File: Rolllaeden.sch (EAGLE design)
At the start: 62 parts, among them IC1 PCF8574P, IC2 PCF8574P, IC3 74HCT04N, IC4 74HCT08N, IC5 74HCT08N, J1 J7MM, J2 J7MM, T1 BC337-25, T2 BC337-25, T3 BC337-25, T4 BC337-25, T5 BC337-25, T6 BC337-25

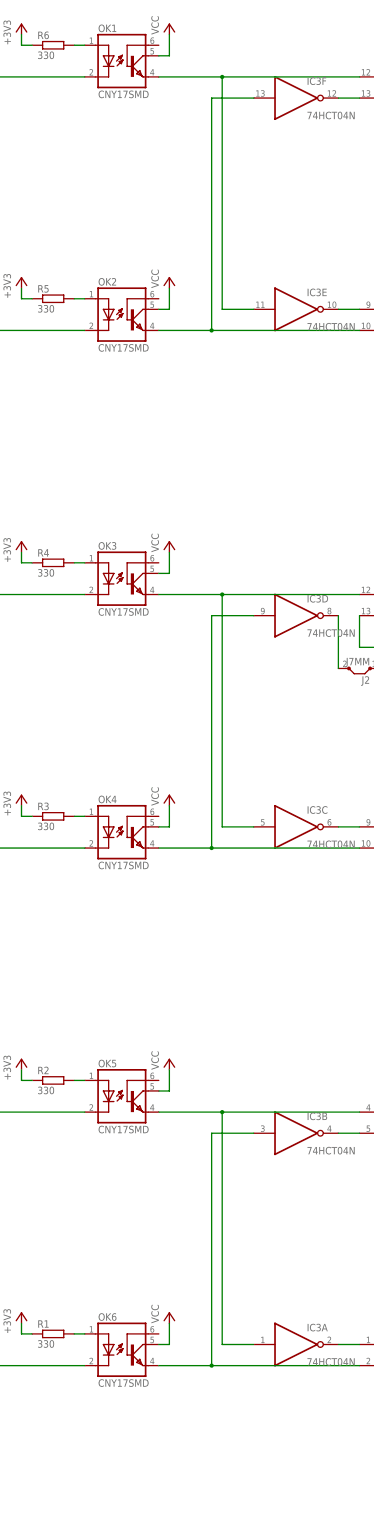
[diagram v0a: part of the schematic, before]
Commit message: Pulldown-Widerstände zwichen Optokopplern und Logik-ICs hinzugefügt
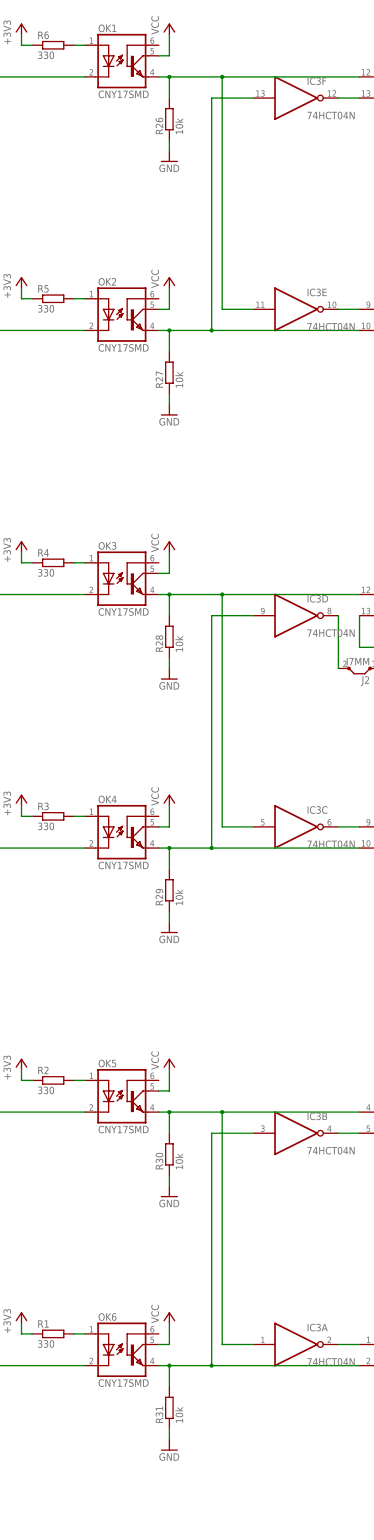
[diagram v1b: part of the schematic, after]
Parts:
- added R26, R27, R28, R29, R30, R31: 10k, resistor:R-EU_0204/2V
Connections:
- net GND: now also R26.1, R27.1, R28.1, R29.1, R30.1, R31.1
- net N$11: now also R30.2
- net N$22: now also R29.2
- net N$23: now also R28.2
- net N$34: now also R27.2
- net N$35: now also R26.2
- net N$4: now also R31.2
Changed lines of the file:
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@@
 <part name="+3V11" library="supply1" deviceset="+3V3" device=""/>
 <part name="F1" library="fuse" deviceset="LITTLEFUSE" device="" value="250mA"/>
+<part name="R26" library="resistor" deviceset="R-EU_" device="0204/2V" value="10k"/>
+<part name="GND5" library="supply1" deviceset="GND" device=""/>
+<part name="R27" library="resistor" deviceset="R-EU_" device="0204/2V" value="10k"/>
+<part name="GND7" library="supply1" deviceset="GND" device=""/>
+<part name="R28" library="resistor" deviceset="R-EU_" device="0204/2V" value="10k"/>
+<part name="GND10" library="supply1" deviceset="GND" device=""/>
+<part name="R29" library="resistor" deviceset="R-EU_" device="0204/2V" value="10k"/>
+<part name="GND11" library="supply1" deviceset="GND" device=""/>
+<part name="R30" library="resistor" deviceset="R-EU_" device="0204/2V" value="10k"/>
+<part name="GND14" library="supply1" deviceset="GND" device=""/>
+<part name="R31" library="resistor" deviceset="R-EU_" device="0204/2V" value="10k"/>
+<part name="GND22" library="supply1" deviceset="GND" device=""/>
 </parts>
 <sheets>
@@
 <instance part="+3V11" gate="G$1" x="-55.88" y="88.9"/>
 <instance part="F1" gate="A" x="-104.14" y="106.68"/>
+<instance part="R26" gate="G$1" x="121.92" y="345.44" rot="R90"/>
+<instance part="GND5" gate="1" x="121.92" y="335.28"/>
+<instance part="R27" gate="G$1" x="121.92" y="284.48" rot="R90"/>
+<instance part="GND7" gate="1" x="121.92" y="274.32"/>
+<instance part="R28" gate="G$1" x="121.92" y="220.98" rot="R90"/>
+<instance part="GND10" gate="1" x="121.92" y="210.82"/>
+<instance part="R29" gate="G$1" x="121.92" y="160.02" rot="R90"/>
+<instance part="GND11" gate="1" x="121.92" y="149.86"/>
+<instance part="R30" gate="G$1" x="121.92" y="96.52" rot="R90"/>
+<instance part="GND14" gate="1" x="121.92" y="86.36"/>
+<instance part="R31" gate="G$1" x="121.92" y="35.56" rot="R90"/>
+<instance part="GND22" gate="1" x="121.92" y="25.4"/>
 </instances>
 <busses>
@@
 <wire x1="-109.22" y1="104.14" x2="-116.84" y2="104.14" width="0.1524" layer="91"/>
 </segment>
+<segment>
+<pinref part="GND5" gate="1" pin="GND"/>
+<pinref part="R26" gate="G$1" pin="1"/>
+<wire x1="121.92" y1="337.82" x2="121.92" y2="340.36" width="0.1524" layer="91"/>
+</segment>
+<segment>
+<pinref part="GND7" gate="1" pin="GND"/>
+<pinref part="R27" gate="G$1" pin="1"/>
+<wire x1="121.92" y1="276.86" x2="121.92" y2="279.4" width="0.1524" layer="91"/>
+</segment>
+<segment>
+<pinref part="GND10" gate="1" pin="GND"/>
+<pinref part="R28" gate="G$1" pin="1"/>
+<wire x1="121.92" y1="213.36" x2="121.92" y2="215.9" width="0.1524" layer="91"/>
+</segment>
+<segment>
+<pinref part="GND11" gate="1" pin="GND"/>
+<pinref part="R29" gate="G$1" pin="1"/>
+<wire x1="121.92" y1="152.4" x2="121.92" y2="154.94" width="0.1524" layer="91"/>
+</segment>
+<segment>
+<pinref part="GND14" gate="1" pin="GND"/>
+<pinref part="R30" gate="G$1" pin="1"/>
+<wire x1="121.92" y1="88.9" x2="121.92" y2="91.44" width="0.1524" layer="91"/>
+</segment>
+<segment>
+<pinref part="GND22" gate="1" pin="GND"/>
+<pinref part="R31" gate="G$1" pin="1"/>
+<wire x1="121.92" y1="27.94" x2="121.92" y2="30.48" width="0.1524" layer="91"/>
+</segment>
 </net>
 <net name="N$1" class="0">
@@
 <segment>
 <pinref part="IC5" gate="A" pin="I1"/>
-<wire x1="119.38" y1="45.72" x2="132.08" y2="45.72" width="0.1524" layer="91"/>
+<wire x1="119.38" y1="45.72" x2="121.92" y2="45.72" width="0.1524" layer="91"/>
 <pinref part="OK6" gate="G$1" pin="EMI"/>
 <pinref part="IC3" gate="B" pin="I"/>
+<wire x1="121.92" y1="45.72" x2="132.08" y2="45.72" width="0.1524" layer="91"/>
 <wire x1="132.08" y1="45.72" x2="167.64" y2="45.72" width="0.1524" layer="91"/>
 <wire x1="142.24" y1="101.6" x2="132.08" y2="101.6" width="0.1524" layer="91"/>
 <wire x1="132.08" y1="101.6" x2="132.08" y2="45.72" width="0.1524" layer="91"/>
 <junction x="132.08" y="45.72"/>
+<pinref part="R31" gate="G$1" pin="2"/>
+<wire x1="121.92" y1="40.64" x2="121.92" y2="45.72" width="0.1524" layer="91"/>
+<junction x="121.92" y="45.72"/>
 </segment>
 </net>
@@
 <pinref part="OK5" gate="G$1" pin="EMI"/>
 <pinref part="IC5" gate="B" pin="I0"/>
-<wire x1="119.38" y1="106.68" x2="134.62" y2="106.68" width="0.1524" layer="91"/>
+<wire x1="119.38" y1="106.68" x2="121.92" y2="106.68" width="0.1524" layer="91"/>
 <pinref part="IC3" gate="A" pin="I"/>
+<wire x1="121.92" y1="106.68" x2="134.62" y2="106.68" width="0.1524" layer="91"/>
 <wire x1="134.62" y1="106.68" x2="167.64" y2="106.68" width="0.1524" layer="91"/>
 <wire x1="142.24" y1="50.8" x2="134.62" y2="50.8" width="0.1524" layer="91"/>
 <wire x1="134.62" y1="50.8" x2="134.62" y2="106.68" width="0.1524" layer="91"/>
 <junction x="134.62" y="106.68"/>
+<pinref part="R30" gate="G$1" pin="2"/>
+<wire x1="121.92" y1="101.6" x2="121.92" y2="106.68" width="0.1524" layer="91"/>
+<junction x="121.92" y="106.68"/>
 </segment>
 </net>
@@
 <wire x1="167.64" y1="170.18" x2="132.08" y2="170.18" width="0.1524" layer="91"/>
 <pinref part="IC3" gate="D" pin="I"/>
-<wire x1="132.08" y1="170.18" x2="119.38" y2="170.18" width="0.1524" layer="91"/>
+<wire x1="132.08" y1="170.18" x2="121.92" y2="170.18" width="0.1524" layer="91"/>
+<wire x1="121.92" y1="170.18" x2="119.38" y2="170.18" width="0.1524" layer="91"/>
 <wire x1="142.24" y1="226.06" x2="132.08" y2="226.06" width="0.1524" layer="91"/>
 <wire x1="132.08" y1="226.06" x2="132.08" y2="170.18" width="0.1524" layer="91"/>
 <junction x="132.08" y="170.18"/>
+<pinref part="R29" gate="G$1" pin="2"/>
+<wire x1="121.92" y1="165.1" x2="121.92" y2="170.18" width="0.1524" layer="91"/>
+<junction x="121.92" y="170.18"/>
 </segment>
 </net>
@@
 <pinref part="OK3" gate="G$1" pin="EMI"/>
 <pinref part="IC5" gate="D" pin="I0"/>
-<wire x1="119.38" y1="231.14" x2="134.62" y2="231.14" width="0.1524" layer="91"/>
+<wire x1="119.38" y1="231.14" x2="121.92" y2="231.14" width="0.1524" layer="91"/>
 <pinref part="IC3" gate="C" pin="I"/>
+<wire x1="121.92" y1="231.14" x2="134.62" y2="231.14" width="0.1524" layer="91"/>
 <wire x1="134.62" y1="231.14" x2="167.64" y2="231.14" width="0.1524" layer="91"/>
 <wire x1="142.24" y1="175.26" x2="134.62" y2="175.26" width="0.1524" layer="91"/>
 <wire x1="134.62" y1="175.26" x2="134.62" y2="231.14" width="0.1524" layer="91"/>
 <junction x="134.62" y="231.14"/>
+<pinref part="R28" gate="G$1" pin="2"/>
+<wire x1="121.92" y1="226.06" x2="121.92" y2="231.14" width="0.1524" layer="91"/>
+<junction x="121.92" y="231.14"/>
 </segment>
 </net>
@@
 <pinref part="OK2" gate="G$1" pin="EMI"/>
 <wire x1="167.64" y1="294.64" x2="132.08" y2="294.64" width="0.1524" layer="91"/>
-<wire x1="132.08" y1="294.64" x2="119.38" y2="294.64" width="0.1524" layer="91"/>
+<wire x1="132.08" y1="294.64" x2="121.92" y2="294.64" width="0.1524" layer="91"/>
+<wire x1="121.92" y1="294.64" x2="119.38" y2="294.64" width="0.1524" layer="91"/>
 <wire x1="142.24" y1="350.52" x2="132.08" y2="350.52" width="0.1524" layer="91"/>
 <wire x1="132.08" y1="350.52" x2="132.08" y2="294.64" width="0.1524" layer="91"/>
@@
 <pinref part="IC3" gate="F" pin="I"/>
 <pinref part="IC4" gate="C" pin="I1"/>
+<pinref part="R27" gate="G$1" pin="2"/>
+<wire x1="121.92" y1="289.56" x2="121.92" y2="294.64" width="0.1524" layer="91"/>
+<junction x="121.92" y="294.64"/>
 </segment>
 </net>
@@
 <segment>
 <pinref part="OK1" gate="G$1" pin="EMI"/>
-<wire x1="119.38" y1="355.6" x2="134.62" y2="355.6" width="0.1524" layer="91"/>
+<wire x1="119.38" y1="355.6" x2="121.92" y2="355.6" width="0.1524" layer="91"/>
+<wire x1="121.92" y1="355.6" x2="134.62" y2="355.6" width="0.1524" layer="91"/>
 <wire x1="134.62" y1="355.6" x2="167.64" y2="355.6" width="0.1524" layer="91"/>
 <wire x1="142.24" y1="299.72" x2="134.62" y2="299.72" width="0.1524" layer="91"/>
@@
 <pinref part="IC3" gate="E" pin="I"/>
 <pinref part="IC4" gate="D" pin="I0"/>
-</segment>
-</net>
+<pinref part="R26" gate="G$1" pin="2"/>
+<wire x1="121.92" y1="350.52" x2="121.92" y2="355.6" width="0.1524" layer="91"/>
+<junction x="121.92" y="355.6"/>
+</segment>
+</net>

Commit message: Schaltpläne aufgehübscht zur Veröffentlichung
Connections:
- net N$16 renamed SIG_RR
- net N$32 renamed SIG_MH
- net N$33 renamed SIG_MR
- net N$36 renamed SIG_LH
- net N$37 renamed SIG_LR
- net N$47 renamed T_LR
- net N$48 renamed T_LH
- net N$50 renamed T_MR
- net N$51 renamed T_MH
- net N$56 renamed T_RR
- net N$57 renamed T_RH
- net N$99 renamed SIG_RH
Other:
- note added: "HomePi - Rollladensteuerung Rev. 2015/12a Ausgänge"
- note added: "HomePi - Rollladensteuerung Rev. 2015/12a Eingänge"
- note added: "HomePi - Rollladensteuerung Rev. 2015/12a ICs"
